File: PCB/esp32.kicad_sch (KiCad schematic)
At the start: 36 parts, among them J1 USB_C, J14 PWR_CONN, J15 SPI_0, J16 SPI_1, J3 A0, J4 A1, J5 A2, J6 D0, J7 D1, J8 USB_VOUT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

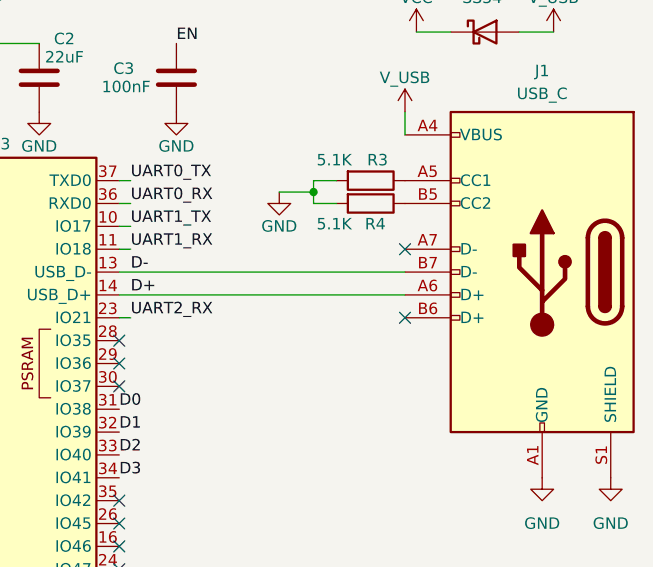
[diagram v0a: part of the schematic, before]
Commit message: fix usb differential pair
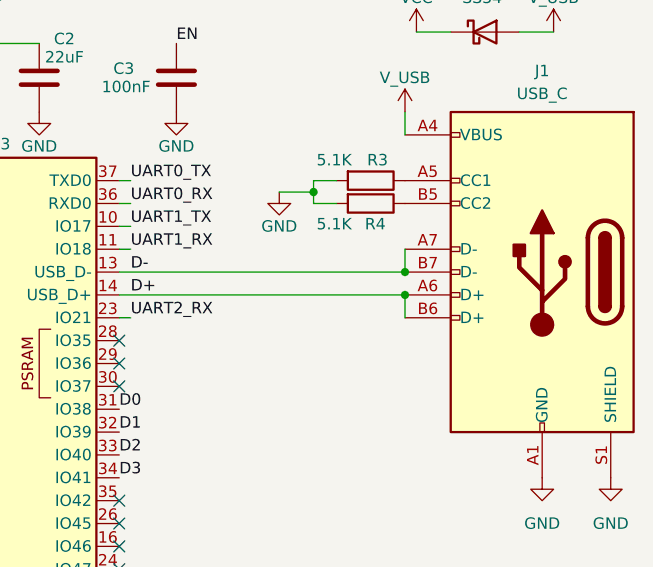
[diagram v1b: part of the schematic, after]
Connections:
- net D+: now also J1.B6 (D+)
- net D-: now also J1.A7 (D-)
- no-connect marks 10 -> 8
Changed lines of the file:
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@@
+	)
+	(junction
+		(at 254 52.07)
+		(diameter 0)
+		(color 0 0 0 0)
 	)
 	(junction
@@
 	)
 	(junction
+		(at 254 49.53)
+		(diameter 0)
+		(color 0 0 0 0)
+	)
+	(junction
 		(at 102.87 30.48)
 		(diameter 0)
@@
 	)
 	(no_connect
-		(at 254 54.61)
-	)
-	(no_connect
-		(at 254 46.99)
-	)
-	(no_connect
 		(at 191.77 52.07)
 	)
@@
 	(wire
 		(pts
+			(xy 254 46.99) (xy 254 49.53)
+		)
+		(stroke
+			(width 0)
+			(type default)
+		)
+	)
+	(wire
+		(pts
 			(xy 254 31.75) (xy 254 34.29)
 		)
@@
 		)
 		(stroke
+			(width 0)
+			(type default)
+		)
+	)
+	(wire
+		(pts
+			(xy 254 52.07) (xy 254 54.61)
+		)
+		(stroke
